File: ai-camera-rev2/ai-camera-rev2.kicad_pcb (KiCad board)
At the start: 4 copper layers, 70 x 70 mm, 176 parts, among them J1 Conn-01x02_P2mm_NONAME_JST-PH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, J2 TYPE-C-31-M-12, J3 MAXLAB, J4 Conn-02x10_P2.54mm_B-2100S20P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, J5 Conn-01x02_P1.25mm_10114829-1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, J6 Conn_01x24_FFC_0.5mm_AFC01-S2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, Q1 2N7002, Q2 2N7002, Q3 AO3401A, Q4 AO3401A, Q5 2N7002, Q6 AO3401A, Q7 2N7002, Q8 AO3401A, Q9 2N7002, SW1 SW_PB_90deg_K2-1102AQ-H4CW-01, SW2 SW_PB_TS-1187A-B-A-B, SW3 SW_PB_TS-1187A-B-A-B, SW4 SW_PB_90deg_K2-1102AQ-H4CW-01, U1 TP4057-42-SOT26-R, U10 ESP32-S3-WROOM-1-N16R8, U11 MT9284-28J, U12 LTR-303ALS-01, U2 XC6206-2.8V, U3 PCF85063AT_SO8, U4 SOT-23-6_SN74LVC1G373DBVR_TI, U5 SY8089AAAC, U6 PIR_AS312, U7 XC6206-2.8V, U8 RT9166-12GVL, U9 AP1511B, Y1 32.768kHz_Q13FC1350000400

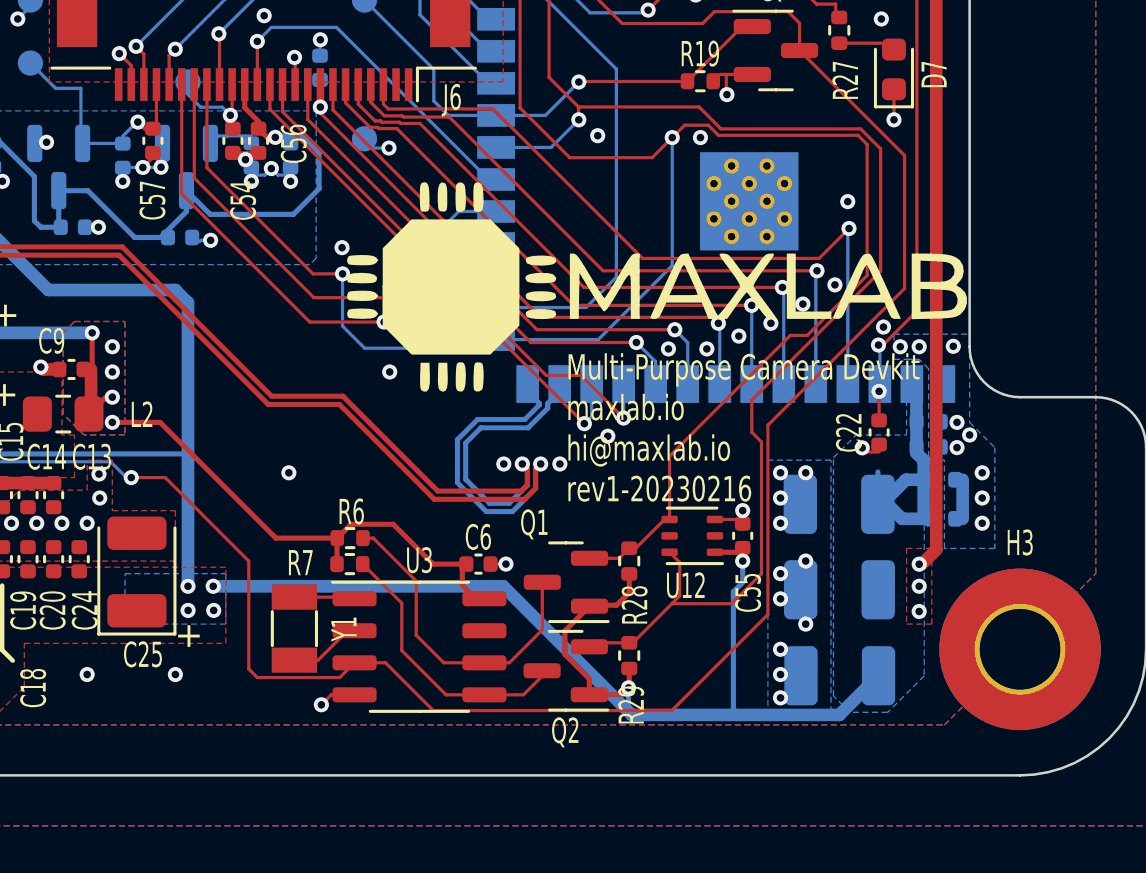
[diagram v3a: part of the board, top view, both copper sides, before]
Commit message: EAC-49: better caps placement near ESP32
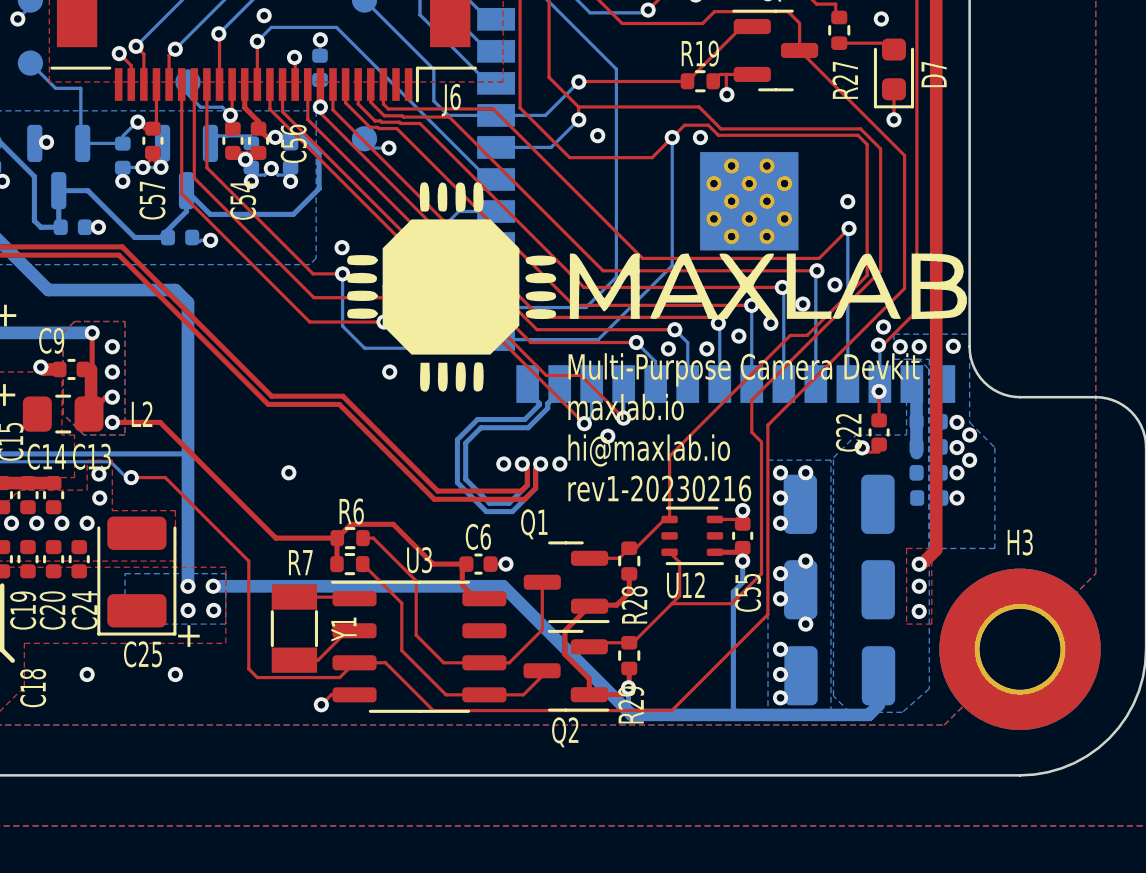
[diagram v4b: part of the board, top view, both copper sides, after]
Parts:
- moved C42 0.99 mm to (156.4, 104.0)
- moved C44 0.64 mm to (156.4, 103.0)
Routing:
- net +3V3: track 200.0 -> 193.0 mm
- net GND: track 89.5 -> 88.6 mm
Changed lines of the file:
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@@
     (property "ki_keywords" "cap capacitor 25V 10% 0402")
     (attr smd)
-    (fp_text reference "C46" (at 3.375 0.775) (layer "B.SilkS")
+    (fp_text reference "C46" (at 3.025 0.625) (layer "B.SilkS")
         (effects (font (size 1 0.6) (thickness 0.15)) (justify mirror))
     )
@@
     (property "ki_keywords" "cap capacitor 25V 10% 0402")
     (attr smd)
-    (fp_text reference "C47" (at 3.375 0.525) (layer "B.SilkS")
+    (fp_text reference "C47" (at 3.025 0.325) (layer "B.SilkS")
         (effects (font (size 1 0.6) (thickness 0.15)) (justify mirror))
     )
@@
   )
   (footprint "Capacitor_SMD:C_0402_1005Metric" (layer "B.Cu")
-    (at 156.95 104.825)
+    (at 156.4 104)
     (descr "Capacitor SMD 0402 (1005 Metric), square (rectangular) end terminal, IPC_7351 nominal, (Body size source: IPC-SM-782 page 76, https://www.pcb-3d.com/wordpress/wp-content/uploads/ipc-sm-782a_amendment_1_and_2.pdf), generated with kicad-footprint-generator")
     (tags "capacitor")
@@
     (property "ki_keywords" "cap capacitor 25V 10% 0402")
     (attr smd)
-    (fp_text reference "C42" (at 2.8 0.425 180) (layer "B.SilkS")
+    (fp_text reference "C42" (at 3 1.2 180) (layer "B.SilkS")
         (effects (font (size 1 0.6) (thickness 0.15)) (justify mirror))
     )
@@
   )
   (footprint "Capacitor_SMD:C_0402_1005Metric" (layer "B.Cu")
-    (at 156.95 103.275)
+    (at 156.375 103)
     (descr "Capacitor SMD 0402 (1005 Metric), square (rectangular) end terminal, IPC_7351 nominal, (Body size source: IPC-SM-782 page 76, https://www.pcb-3d.com/wordpress/wp-content/uploads/ipc-sm-782a_amendment_1_and_2.pdf), generated with kicad-footprint-generator")
     (tags "capacitor")
@@
     (property "ki_keywords" "cap capacitor 25V 10% 0402")
     (attr smd)
-    (fp_text reference "C44" (at 2.8 0.725 180) (layer "B.SilkS")
+    (fp_text reference "C44" (at 3.025 0.9 180) (layer "B.SilkS")
         (effects (font (size 1 0.6) (thickness 0.15)) (justify mirror))
     )
@@
   (segment (start 131.25 87.6) (end 131.25 86.55) (width 0.127) (layer "F.Cu") (net 1))
   (segment (start 154.41 102.175) (end 153.905 102.175) (width 0.127) (layer "F.Cu") (net 1))
+  (segment (start 125.607 90.311) (end 125.607 90.557) (width 0.127) (layer "F.Cu") (net 1))
   (segment (start 148.35 87.2) (end 148.35 87.975) (width 0.127) (layer "F.Cu") (net 1))
   (segment (start 105.0075 85.6825) (end 105.35 86.025) (width 0.127) (layer "F.Cu") (net 1))
@@
   (segment (start 113.78 105) (end 116.75 105) (width 0.127) (layer "F.Cu") (net 1))
   (segment (start 102.725 90.69) (end 102.725 90.225) (width 0.127) (layer "F.Cu") (net 1))
+  (segment (start 125.607 90.557) (end 125.93 90.88) (width 0.127) (layer "F.Cu") (net 1))
   (segment (start 131.25 86.55) (end 131.225 86.525) (width 0.127) (layer "F.Cu") (net 1))
   (segment (start 101.725 81.25) (end 102.475 80.5) (width 0.5) (layer "F.Cu") (net 1))
@@
   (via (at 128 80.5) (size 0.6) (drill 0.3) (layers "F.Cu" "B.Cu") (net 1))
   (via (at 144.25 58.5) (size 0.6) (drill 0.3) (layers "F.Cu" "B.Cu") (net 1))
-  (via (at 158.5 105) (size 0.6) (drill 0.3) (layers "F.Cu" "B.Cu") (free) (net 1))
+  (via (at 158 102.5) (size 0.6) (drill 0.3) (layers "F.Cu" "B.Cu") (free) (net 1))
   (via (at 116 89) (size 0.6) (drill 0.3) (layers "F.Cu" "B.Cu") (net 1))
   (via (at 105.75 85) (size 0.6) (drill 0.3) (layers "F.Cu" "B.Cu") (free) (net 1))
@@
   (via (at 109.9 97.3) (size 0.6) (drill 0.3) (layers "F.Cu" "B.Cu") (free) (net 1))
   (via (at 143.25 89.629123) (size 0.6) (drill 0.3) (layers "F.Cu" "B.Cu") (free) (net 1))
-  (via (at 158.5 104) (size 0.6) (drill 0.3) (layers "F.Cu" "B.Cu") (free) (net 1))
-  (via (at 158.5 103) (size 0.6) (drill 0.3) (layers "F.Cu" "B.Cu") (free) (net 1))
+  (via (at 157.5 104) (size 0.6) (drill 0.3) (layers "F.Cu" "B.Cu") (free) (net 1))
+  (via (at 157.5 103) (size 0.6) (drill 0.3) (layers "F.Cu" "B.Cu") (free) (net 1))
   (via (at 126.5 111) (size 0.6) (drill 0.3) (layers "F.Cu" "B.Cu") (net 1))
   (via (at 119.384 70.908) (size 0.6) (drill 0.3) (layers "F.Cu" "B.Cu") (free) (net 1))
@@
   (segment (start 141.3 80.44) (end 141.981257 80.44) (width 0.127) (layer "B.Cu") (net 1))
   (segment (start 114.74 55.57) (end 113.37 55.57) (width 0.127) (layer "B.Cu") (net 1))
-  (segment (start 157.725 103.275) (end 157.725 104.825) (width 0.5) (layer "B.Cu") (net 1))
   (segment (start 149.102 78.762) (end 148.99 78.65) (width 0.127) (layer "B.Cu") (net 1))
   (segment (start 117.5 47.75) (end 111.25 54) (width 0.5) (layer "F.Cu") (net 3))
@@
   (segment (start 127 102.25) (end 115.5 102.25) (width 0.2032) (layer "B.Cu") (net 6))
   (segment (start 148.73 112.6025) (end 144.6025 112.6025) (width 0.5) (layer "B.Cu") (net 6))
-  (segment (start 155.895 102.22) (end 156.175 102.5) (width 0.5) (layer "B.Cu") (net 6))
   (segment (start 148.63 107.72) (end 149 107.35) (width 0.2032) (layer "B.Cu") (net 6))
   (segment (start 150.75 53.5) (end 149.75 54.5) (width 0.5) (layer "B.Cu") (net 6))
+  (segment (start 153.9975 112.6025) (end 148.73 112.6025) (width 0.5) (layer "B.Cu") (net 6))
   (segment (start 116.27 68.77) (end 115.75 68.77) (width 0.5) (layer "B.Cu") (net 6))
-  (segment (start 156.175 103.275) (end 156.175 102.5) (width 0.5) (layer "B.Cu") (net 6))
+  (segment (start 154.3875 111.05) (end 154.3875 112.2125) (width 0.5) (layer "B.Cu") (net 6))
   (segment (start 117.0458 91.7958) (end 116.4238 91.1738) (width 0.5) (layer "B.Cu") (net 6))
-  (segment (start 152.835 112.6025) (end 148.73 112.6025) (width 0.5) (layer "B.Cu") (net 6))
   (segment (start 127 96.25) (end 127 102.25) (width 0.5) (layer "B.Cu") (net 6))
   (segment (start 149.75 54.5) (end 149.75 57) (width 0.5) (layer "B.Cu") (net 6))
   (segment (start 144.47 111.53) (end 144.47 112.47) (width 0.2032) (layer "B.Cu") (net 6))
   (segment (start 114 90.67) (end 114 88.5) (width 0.5) (layer "B.Cu") (net 6))
-  (segment (start 155.325 104.825) (end 154.75 104.25) (width 0.5) (layer "B.Cu") (net 6))
   (segment (start 115.75 68.77) (end 113.205 68.77) (width 0.5) (layer "B.Cu") (net 6))
   (segment (start 148 59.5) (end 148 60.75) (width 0.5) (layer "B.Cu") (net 6))
@@
   (segment (start 114.761 102.239) (end 114 103) (width 0.2032) (layer "B.Cu") (net 6))
   (segment (start 149.825 57.075) (end 149.75 57) (width 0.5) (layer "B.Cu") (net 6))
+  (segment (start 154.3875 112.2125) (end 153.9975 112.6025) (width 0.5) (layer "B.Cu") (net 6))
   (segment (start 149.75 57.75) (end 148 59.5) (width 0.5) (layer "B.Cu") (net 6))
   (segment (start 146.25 60.75) (end 148 60.75) (width 0.5) (layer "B.Cu") (net 6))
   (segment (start 117 71.25) (end 117 69.5) (width 0.5) (layer "B.Cu") (net 6))
-  (segment (start 156.175 104.825) (end 156.175 103.275) (width 0.5) (layer "B.Cu") (net 6))
   (segment (start 158 76.5) (end 157 75.5) (width 0.5) (layer "B.Cu") (net 6))
   (segment (start 155.895 101.975) (end 155.895 102.22) (width 0.5) (layer "B.Cu") (net 6))
@@
   (segment (start 115.489 102.239) (end 114.761 102.239) (width 0.2032) (layer "B.Cu") (net 6))
   (segment (start 155.895 100.975) (end 155.895 99.665) (width 0.5) (layer "B.Cu") (net 6))
-  (segment (start 156.175 104.825) (end 155.325 104.825) (width 0.5) (layer "B.Cu") (net 6))
   (segment (start 154.968 63.468) (end 150.718 63.468) (width 0.5) (layer "B.Cu") (net 6))
   (segment (start 126.5 95.75) (end 127 96.25) (width 0.5) (layer "B.Cu") (net 6))
@@
   (segment (start 114.5038 91.1738) (end 114 90.67) (width 0.5) (layer "B.Cu") (net 6))
   (segment (start 117.448 85.052) (end 117.448 82.131354) (width 0.5) (layer "B.Cu") (net 6))
-  (segment (start 155.475 103.275) (end 154.5 104.25) (width 0.5) (layer "B.Cu") (net 6))
   (segment (start 117.5044 91.7958) (end 121.4586 95.75) (width 0.5) (layer "B.Cu") (net 6))
   (segment (start 117.448 82.131354) (end 118 81.579354) (width 0.5) (layer "B.Cu") (net 6))
@@
   (segment (start 117.5044 91.7958) (end 117.0458 91.7958) (width 0.5) (layer "B.Cu") (net 6))
   (segment (start 149.75 57) (end 149.75 57.75) (width 0.5) (layer "B.Cu") (net 6))
-  (segment (start 154.3875 111.05) (end 152.835 112.6025) (width 0.5) (layer "B.Cu") (net 6))
   (segment (start 157 65.5) (end 154.968 63.468) (width 0.5) (layer "B.Cu") (net 6))
   (segment (start 114 88.5) (end 117.448 85.052) (width 0.5) (layer "B.Cu") (net 6))
   (segment (start 114.2 67.3375) (end 114.2 68.675) (width 0.5) (layer "B.Cu") (net 6))
-  (segment (start 154.3625 102.9675) (end 154.3625 104.25) (width 0.2032) (layer "B.Cu") (net 6))
   (segment (start 139.5 107.5) (end 128 107.5) (width 0.5) (layer "B.Cu") (net 6))
-  (segment (start 156.175 103.275) (end 155.475 103.275) (width 0.5) (layer "B.Cu") (net 6))
   (segment (start 121.4586 95.75) (end 126.5 95.75) (width 0.5) (layer "B.Cu") (net 6))
   (segment (start 117 69.5) (end 116.27 68.77) (width 0.5) (layer "B.Cu") (net 6))
@@
   (zone (net 6) (net_name "+3V3") (layer "B.Cu") (hatch edge 0.508)
     (priority 16)
-    (connect_pads (clearance 0.254))
-    (min_thickness 0.254) (filled_areas_thickness no)
-    (fill yes (thermal_gap 0.254) (thermal_bridge_width 0.5))
+    (connect_pads (clearance 0.2))
+    (min_thickness 0.2) (filled_areas_thickness no)
+    (fill yes (thermal_gap 0.2) (thermal_bridge_width 0.5))
     (polygon
       (pts
         (xy 155.5 98.5)
-        (xy 155.75 98.5)
-        (xy 155.75 102.325)
-        (xy 156.2 102.775)
-        (xy 156.2 111.05)
-        (xy 154.75 112.5)
+        (xy 156.4 98.5)
+        (xy 156.4 111.562121)
+        (xy 155.332759 112.5)
         (xy 153.25 112.5)
         (xy 152.6 111.85)
@@
         (xy 159 102)
         (xy 159 106)
-        (xy 157 106)
-        (xy 157 102.5)
-        (xy 156.5 102.5)
-        (xy 156.375 102.375)
+        (xy 156.4 106)
         (xy 156.375 98.875)
         (xy 156 98.5)

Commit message: EAC-49: add power-on detection in case of user button press
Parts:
- added Q9: 2N7002, Package_TO_SOT_SMD:SOT-23, B.Cu at (132.0, 55.0)
- added R22: 215k_0402_0402WGD2153TCE, Resistor_SMD:R_0402_1005Metric, B.Cu at (135.0, 53.8)
- JP2: value SolderJumper_2_Bridged -> PIR
- moved C32 0.49 mm to (156.2, 79.9)
- renumbered Q9 to Q10, R22 to R25, R25 to R26, R26 to R27, R27 to R28, R28 to R29, R29 to R30, R30 to R31, R31 to R32, R32 to R33
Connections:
- J4 pad 18: /IO2 -> GND
- SW1 pad 1: Net-(Q5-D) -> VBUS
- SW1 pad 2: GND -> /PWRON_DET
- U10 pad 38: /IO2 -> /PWRON_DET
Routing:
- net /PWRON_DET: track 0.00 -> 81.5 mm
- net /IO2: track 5.22 -> 0.00 mm
- net GND: track 88.6 -> 93.0 mm, vias 201 -> 203
- net VBUS: track 208.5 -> 210.3 mm
- net /BATT_DETECT: track 76.6 -> 75.5 mm
- net Net-(D13-K): track 34.2 -> 33.5 mm
- net Net-(Q5-D): track 148.1 -> 147.6 mm, vias 4 -> 5

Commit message: EAC-49: fix battery labels
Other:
- board text removed: "IO2"
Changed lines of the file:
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@@
     )
   )
-  (gr_line (start 156.388 57.112) (end 156.388 74.384)
+  (gr_line (start 156.388 59.6) (end 156.388 81.2)
     (stroke (width 0.1778) (type solid)) (layer "F.SilkS"))
-  (gr_line (start 156.388 74.384) (end 155.88 74.384)
+  (gr_line (start 155.88 81.2) (end 156.388 81.2)
     (stroke (width 0.1778) (type solid)) (layer "F.SilkS"))
-  (gr_line (start 155.88 79.464) (end 156.388 79.464)
-    (stroke (width 0.1778) (type solid)) (layer "F.SilkS"))
-  (gr_line (start 155.88 57.112) (end 156.388 57.112)
+  (gr_line (start 155.846 59.6) (end 156.354 59.6)
     (stroke (width 0.1778) (type solid)) (layer "F.SilkS"))
   (gr_line (start 119.63 110.03) (end 119.63 107.47)
@@
   (gr_line (start 120.05 110.45) (end 119.63 110.03)
     (stroke (width 0.1778) (type default)) (layer "F.SilkS"))
-  (gr_line (start 156.75 73.5) (end 156.5 73.5)
-    (stroke (width 0.1778) (type solid)) (layer "F.SilkS"))
   (gr_line (start 167 80) (end 141 80)
     (stroke (width 0.15) (type default)) (layer "Dwgs.User"))
@@
     (effects (font (size 1 0.6) (thickness 0.15)) (justify right))
   )
-  (gr_text "GND" (at 156.61 78.33) (layer "F.SilkS")
+  (gr_text "GND" (at 156.5 58.2 90) (layer "F.SilkS")
     (effects (font (size 1 0.6) (thickness 0.15)))
   )
@@
     (effects (font (size 1 0.6) (thickness 0.15) bold) (justify left bottom))
   )
-  (gr_text "VBUS" (at 156.388 55.588 90) (layer "F.SilkS")
+  (gr_text "VBUS" (at 156.5 55.6 90) (layer "F.SilkS")
     (effects (font (size 1 0.6) (thickness 0.15)))
   )
@@
     (effects (font (size 1 0.6) (thickness 0.15)) (justify right))
   )
-  (gr_text "IO2" (at 156.58 76.45) (layer "F.SilkS")
-    (effects (font (size 1 0.6) (thickness 0.15)))
-  )
   (gr_text "SCL" (at 150.18 68.305) (layer "F.SilkS")
     (effects (font (size 1 0.6) (thickness 0.15)) (justify right))
+  )
+  (gr_text "GND" (at 157.2 74.8 90) (layer "F.SilkS")
+    (effects (font (size 1 0.6) (thickness 0.15)))
   )
   (gr_text "BOOT\n" (at 150.292 60.668) (layer "F.SilkS")
@@
     (effects (font (size 1 0.6) (thickness 0.15)) (justify right))
   )
-  (gr_text "+BATT" (at 110.88 94.63) (layer "F.SilkS")
+  (gr_text "+BATT" (at 111.125 100.25) (layer "F.SilkS")
     (effects (font (size 1 0.6) (thickness 0.15) bold) (justify left bottom))
   )
@@
     (effects (font (size 1 0.6) (thickness 0.15)) (justify right))
   )
-  (gr_text "GND" (at 157.23 74.46 90) (layer "F.SilkS")
-    (effects (font (size 1 0.6) (thickness 0.15)))
-  )
-  (gr_text "GND" (at 111.5 100.38) (layer "F.SilkS")
+  (gr_text "GND" (at 111.6 95.74) (layer "F.SilkS")
     (effects (font (size 1 0.6) (thickness 0.15) bold) (justify left bottom))
   )
